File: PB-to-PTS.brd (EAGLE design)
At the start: 66.6 x 22.9 mm, 9 parts, among them J2 PTS-PORT

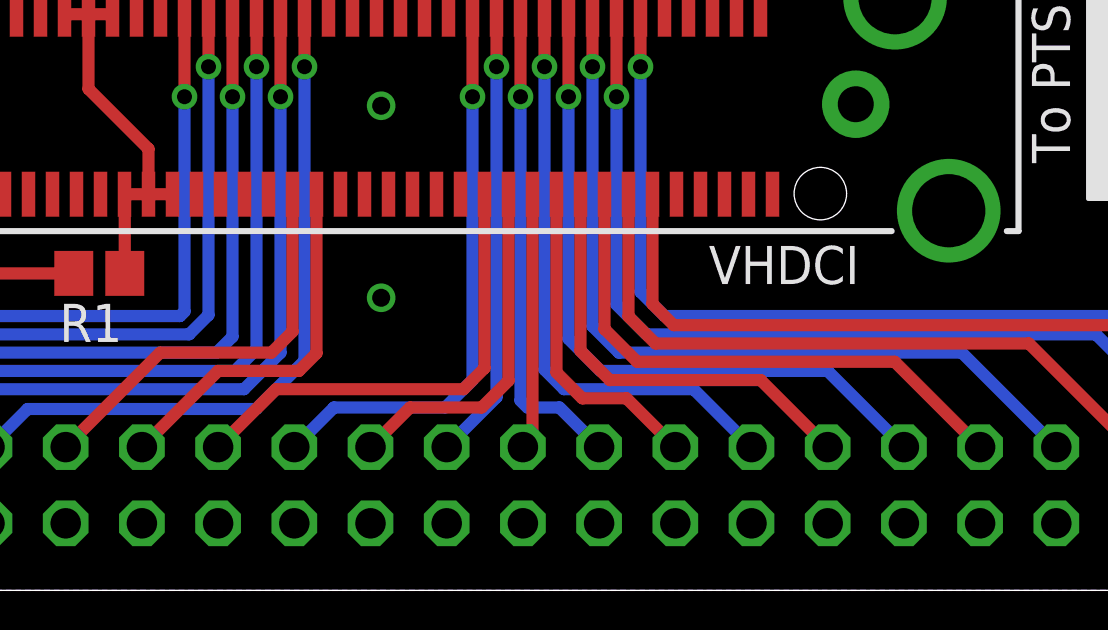
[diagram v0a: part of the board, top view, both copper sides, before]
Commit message: Fix Double-V on board revision, October->Oct
Changed the info block to not automatically include the v, so
the revision no longer prints as 'vv2.0.0'.

Changed the month from 'October 2015' to 'Oct 2015' so it would fit.
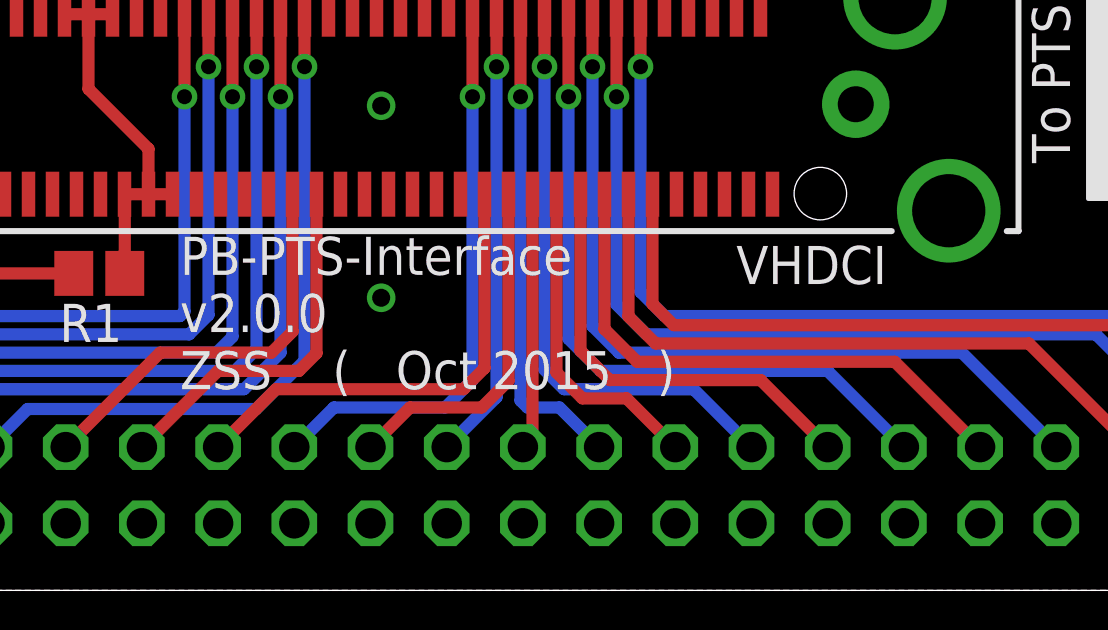
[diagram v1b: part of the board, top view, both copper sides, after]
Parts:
- removed U$2: (no value), PTS_Board_Lib:INFO_BLOCK-0.076
- added U$5: (no value), PTS_Board_Lib:INFO_BLOCK-0.05
- added U$6: (no value), PTS_Board_Lib:INFO_BLOCK-0.076
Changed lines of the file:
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@@
 <text x="11.43" y="20.32" size="1.778" layer="52" rot="MR90">+5V</text>
 <text x="61.4172" y="7.112" size="1.27" layer="26" font="vector" ratio="10" rot="MR0">From PulseBlaster</text>
-<text x="42.3164" y="10.2108" size="1.27" layer="25" font="vector" ratio="10">VHDCI</text>
+<text x="43.2308" y="10.2108" size="1.27" layer="25" font="vector" ratio="10">VHDCI</text>
 <text x="53.086" y="19.558" size="1.27" layer="25" font="vector" ratio="10" rot="R270">To PTS</text>
 </plain>
 <attributes>
 <attribute name="AUTH" value="ZSS"/>
-<attribute name="BRD_MON" value="October 2015"/>
+<attribute name="BRD_MON" value="Oct 2015"/>
 <attribute name="BRD_NAME" value="PB-PTS-Interface"/>
 <attribute name="REV" value="v2.0.0"/>
@@
 <element name="J2" library="PTS_Board_Lib" package="MOLEX-73776-0201" value="PTS-PORT" x="31.0388" y="16.2052"/>
 <element name="R1" library="resistor" package="R0805" value="~200R" x="21.9964" y="10.5664" rot="R180"/>
-<element name="U$2" library="PTS_Board_Lib" package="INFO_BLOCK-0.076" value="" x="43.6372" y="7.5692" rot="MR0"/>
 <element name="LED" library="jumper" package="JP1" value="LED" x="3.6068" y="12.446" rot="MR90"/>
 <element name="QR1" library="QR-git.io-vc0xU" package="QR-HTTP://GIT.IO/VC0XU" value="QR-HTTP://GIT.IO/VC0XU" x="4.6228" y="18.288" smashed="yes" rot="MR0">
@@
 </element>
 <element name="U$3" library="JQI_Logo" package="JQI_LOGO_NEGATIVE-SILKSCREEN" value="" x="54.9656" y="13.0556" smashed="yes"/>
+<element name="U$5" library="PTS_Board_Lib" package="INFO_BLOCK-0.05" value="" x="24.6888" y="6.7056"/>
+<element name="U$6" library="PTS_Board_Lib" package="INFO_BLOCK-0.076" value="" x="40.8432" y="7.0104" rot="MR0"/>
 </elements>
 <signals>
